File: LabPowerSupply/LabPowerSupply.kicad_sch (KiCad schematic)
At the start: 2 parts

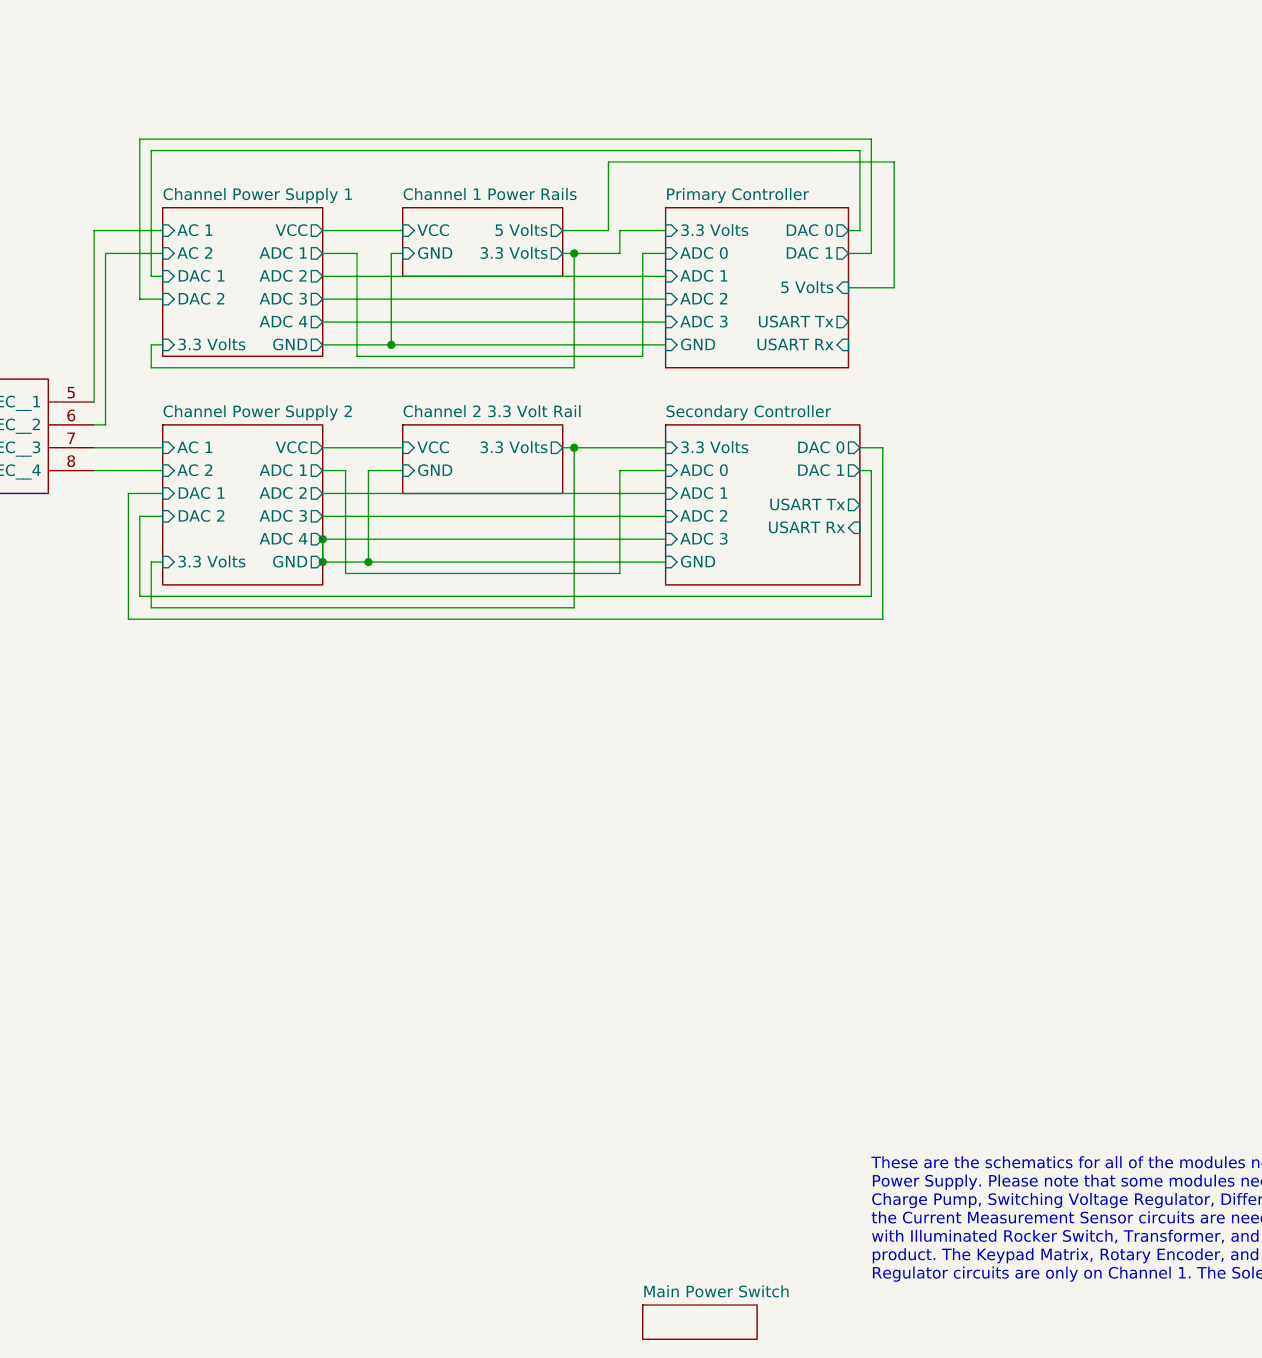
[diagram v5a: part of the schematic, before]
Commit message: added the optocouplers
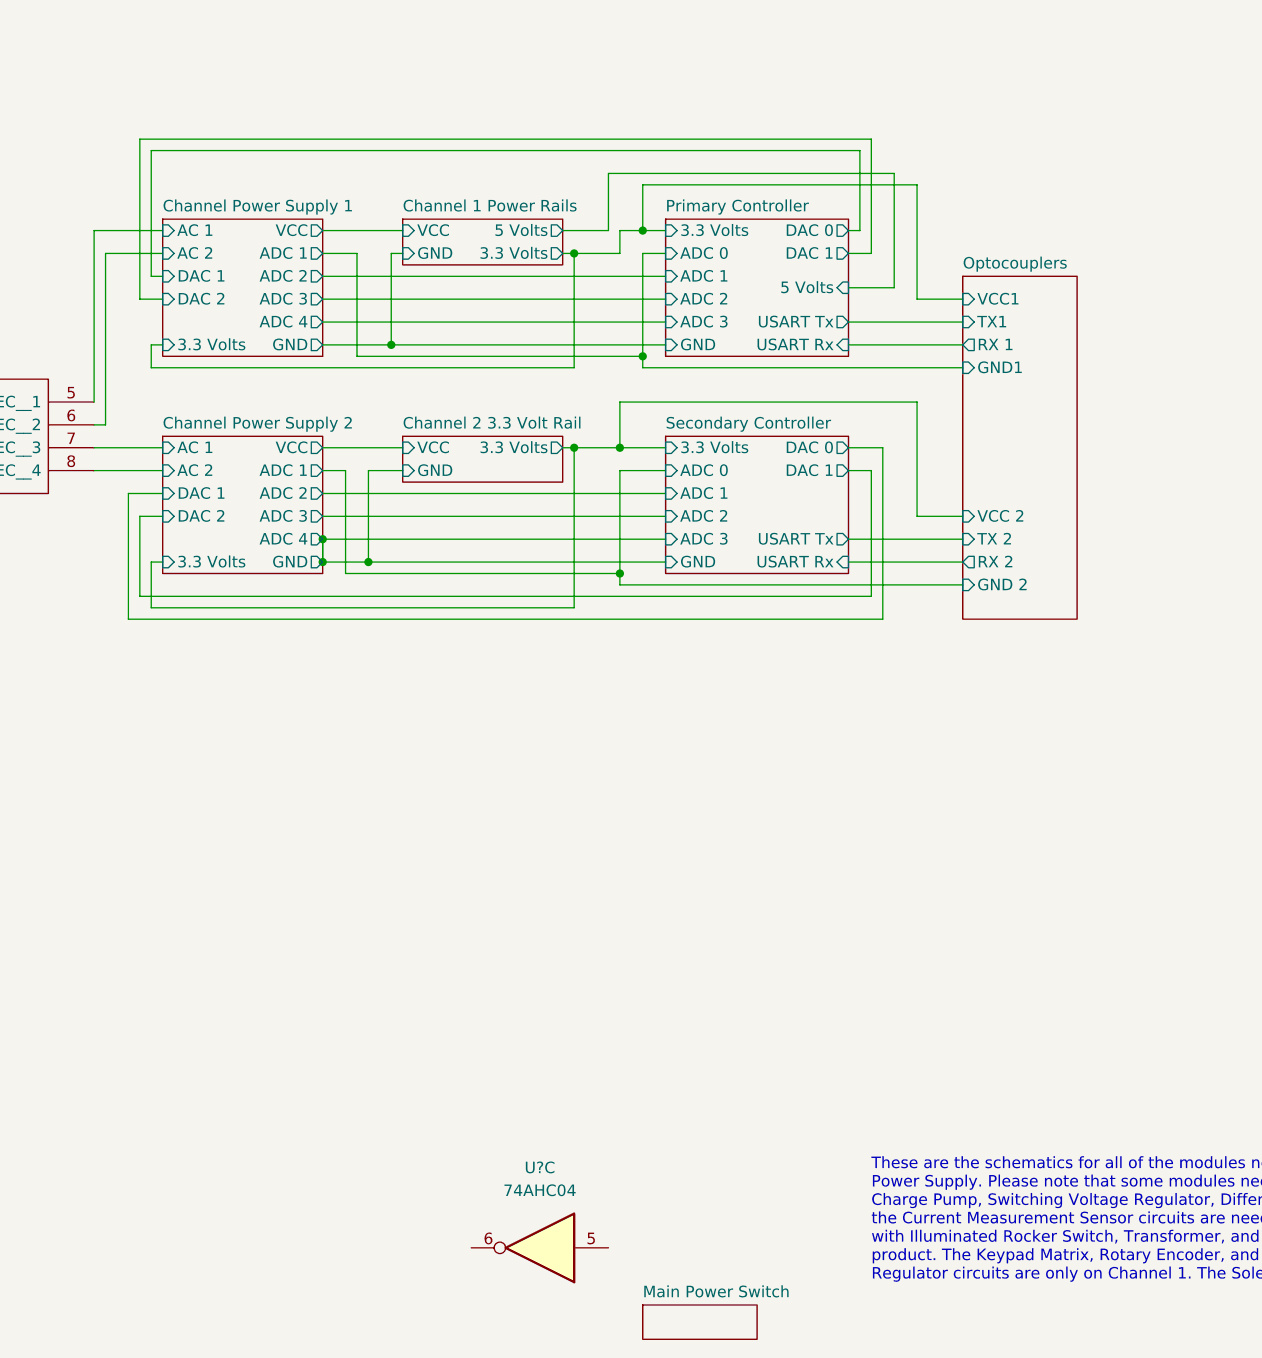
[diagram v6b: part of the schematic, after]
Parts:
- added U?: 74AHC04, symbol 74xx:74AHC04
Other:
- added sheet Optocouplers (Optocouplers.kicad_sch)

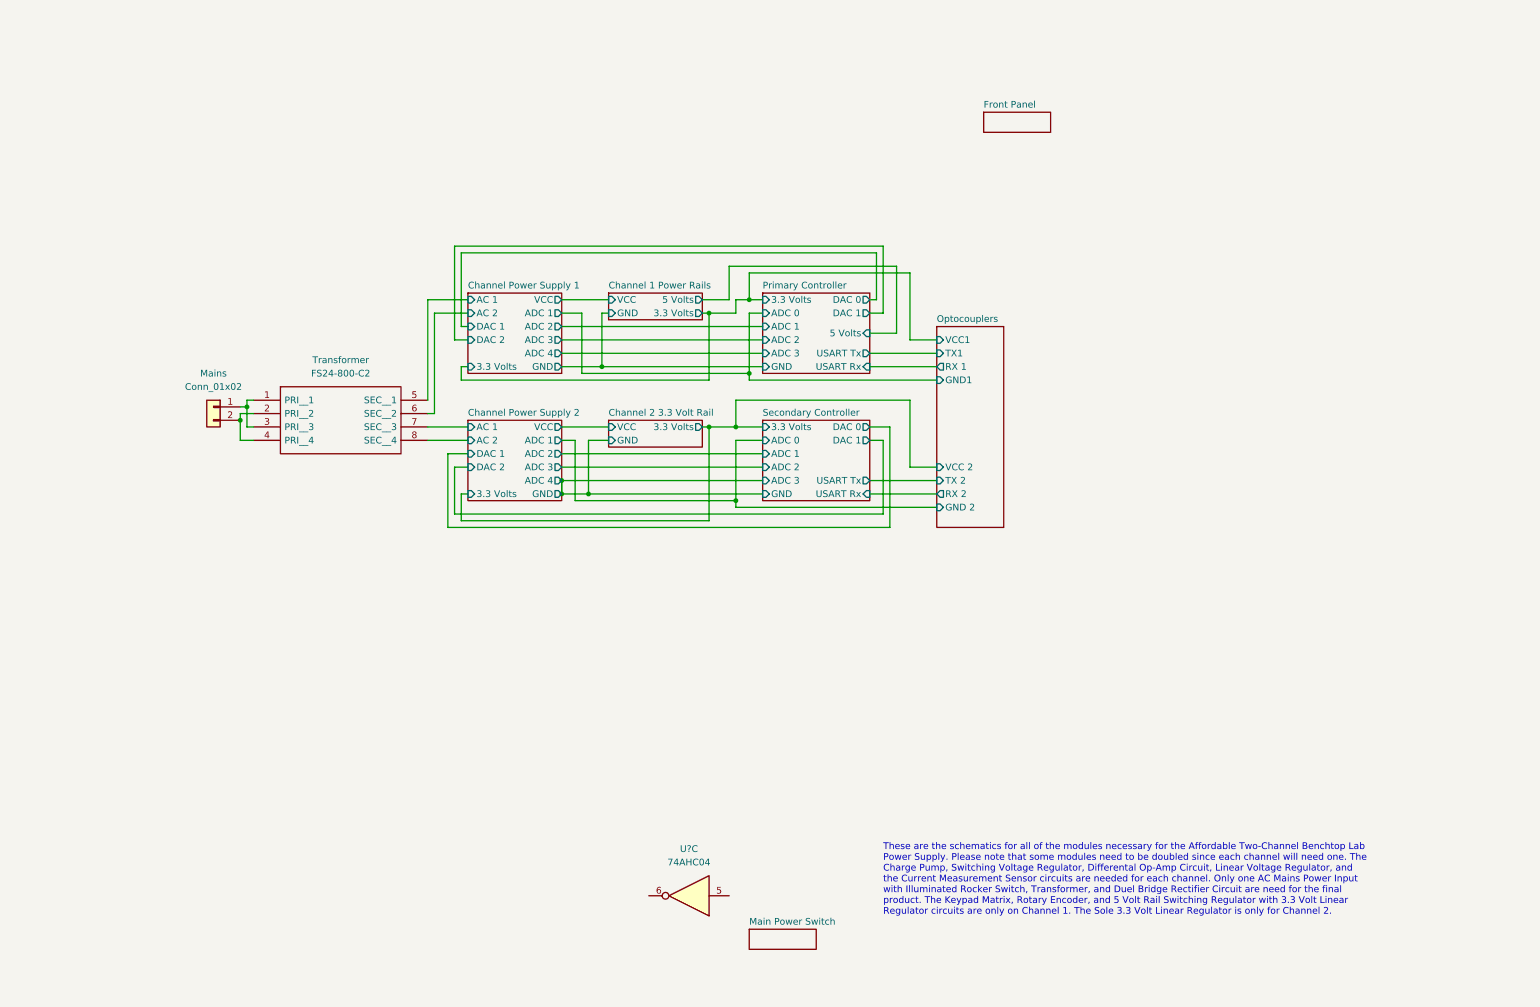
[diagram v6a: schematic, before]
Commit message: Finished first pass on the schematic
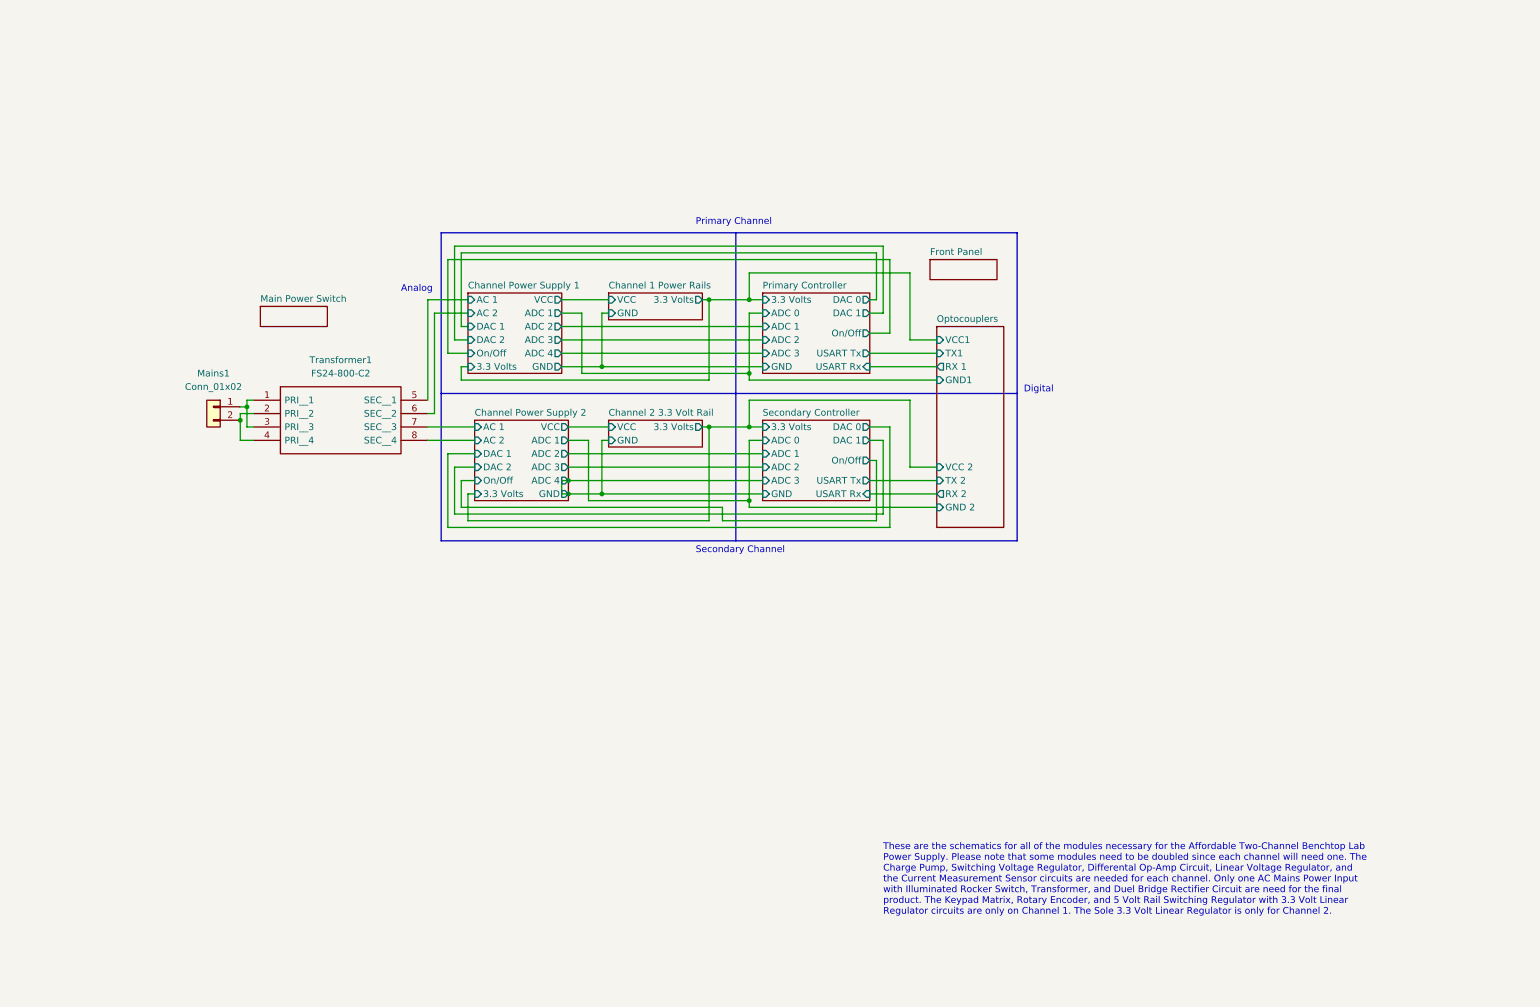
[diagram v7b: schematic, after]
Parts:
- removed U?: 74AHC04, symbol 74xx:74AHC04
- renumbered Mains to Mains1, Transformer to Transformer1
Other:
- sheet Channel 1 Power Rails ports: added none; removed 5 Volts
- sheet Channel Power Supply 1 ports: added On/Off; removed none
- sheet Channel Power Supply 2 ports: added On/Off; removed none
- sheet Primary Controller ports: added On/Off; removed 5 Volts
- sheet Secondary Controller ports: added On/Off; removed none
- note added: "Analog"
- note added: "Digital"
- note added: "Primary Channel"
- note added: "Secondary Channel"

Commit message: started PCB
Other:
- removed sheet Main Power Switch
- note added: "Primary"
- note added: "Secondary"
- note removed: "Primary Channel"
- note removed: "Secondary Channel"
- note removed: "These are the schematics for all of the modules necessary for the Affordable Two-Channel Benchtop Lab Power Supply. Please note that some modules need to be doubled since each channel will need one. The Charge Pump, Switching Voltage Regulator, Differental Op-Amp Circuit, Linear Voltage Regulator, and the Current Measurement Sensor circuits are needed for each channel. Only one AC Mains Power Inp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"
- title: Dual Channel Benchtop Lab Power Supply -> Dual-Channel Benchtop Lab Power Supply
- moved on the sheet: Mains1, Transformer1
